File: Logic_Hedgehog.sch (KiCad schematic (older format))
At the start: 65 parts, among them J40 RaspberryPI3, J41 UART_EXT_1, J42 I2C_EXT_0, J43 I2C_EXT_0_EXP, J44 I2C_EXT_1, J45 SPI_EXT_0_0, J46 SPI_EXT_0_1, J47 SPI_EXT_1, J48 Digital, J49 Analog, J50 Digital, J51 Analog, J52 SERVO, J53 SERVO, J54 MOTORS, J55 MOTORS, U40 STM32F401VBT6, U41 74LVC2G32, U42 MC74VHC1G126, U43 IMU_ICM-20689, U44 DRV8835, U45 DRV8835, U46 Buzzer, Y40 Crystal

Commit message: fixed some footprints, should now be correct and complete
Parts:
- C40, C45, C46, C47, C48, C50, C51, C52, C54, C56, C57, C58: footprint Capacitors_SMD:C_0603_HandSoldering -> Capacitors_SMD:C_0603
- C41, C42, C43, C44: footprint Capacitors_SMD:C_0402 -> Capacitors_SMD:C_0603
- C49, C53, C55: footprint Capacitors_SMD:C_0805_HandSoldering -> Capacitors_SMD:C_0805
- J43: footprint (none) -> Socket_Strips:Socket_Strip_Straight_1x04_Pitch2.54mm
- R40, R41, R42, R45, R46, R47, R48, R49, R50: footprint Resistors_SMD:R_0603_HandSoldering -> Resistors_SMD:R_0603
- R44: footprint Resistors_SMD:R_0402 -> Resistors_SMD:R_0603
- U43: footprint hedgehog_footprints:QFN-24_3x3mm -> Housings_DFN_QFN:QFN-24_4x4mm_Pitch0.5mm
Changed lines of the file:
@@
 LIBS:switches
 LIBS:Hedgehog-cache
-EELAYER 25 0
+EELAYER 26 0
 EELAYER END
 $Descr A3 16535 11693
@@
 F 0 "R48" V 11575 1575 50  0000 C CNN
 F 1 "330R" V 11575 1800 50  0000 C CNN
-F 2 "Resistors_SMD:R_0603_HandSoldering" V 11580 1725 50  0001 C CNN
+F 2 "Resistors_SMD:R_0603" V 11580 1725 50  0001 C CNN
 F 3 "" H 11650 1725 50  0001 C CNN
 	1    11650 1725
@@
 F 0 "R47" V 11575 1375 50  0000 C CNN
 F 1 "330R" V 11575 1600 50  0000 C CNN
-F 2 "Resistors_SMD:R_0603_HandSoldering" V 11580 1525 50  0001 C CNN
+F 2 "Resistors_SMD:R_0603" V 11580 1525 50  0001 C CNN
 F 3 "" H 11650 1525 50  0001 C CNN
 	1    11650 1525
@@
 F 0 "C56" V 14700 2575 50  0000 C CNN
 F 1 "1µ" V 14800 2575 50  0000 C CNN
-F 2 "Capacitors_SMD:C_0603_HandSoldering" H 14788 2300 50  0001 C CNN
+F 2 "Capacitors_SMD:C_0603" H 14788 2300 50  0001 C CNN
 F 3 "" H 14750 2450 50  0001 C CNN
 	1    14750 2450
@@
 F 0 "C57" V 14700 4325 50  0000 C CNN
 F 1 "1µ" V 14800 4325 50  0000 C CNN
-F 2 "Capacitors_SMD:C_0603_HandSoldering" H 14788 4050 50  0001 C CNN
+F 2 "Capacitors_SMD:C_0603" H 14788 4050 50  0001 C CNN
 F 3 "" H 14750 4200 50  0001 C CNN
 	1    14750 4200
@@
 F 0 "C58" V 14700 5650 50  0000 C CNN
 F 1 "1µ" V 14800 5650 50  0000 C CNN
-F 2 "Capacitors_SMD:C_0603_HandSoldering" H 14788 5375 50  0001 C CNN
+F 2 "Capacitors_SMD:C_0603" H 14788 5375 50  0001 C CNN
 F 3 "" H 14750 5525 50  0001 C CNN
 	1    14750 5525
@@
 F 0 "R41" H 7400 9925 50  0000 L CNN
 F 1 "R" H 7400 9850 50  0000 L CNN
-F 2 "Resistors_SMD:R_0603_HandSoldering" V 7280 9900 50  0001 C CNN
+F 2 "Resistors_SMD:R_0603" V 7280 9900 50  0001 C CNN
 F 3 "" H 7350 9900 50  0001 C CNN
 	1    7350 9900
@@
 F 0 "R40" H 3800 6575 50  0000 L CNN
 F 1 "R" H 3800 6475 50  0000 L CNN
-F 2 "Resistors_SMD:R_0603_HandSoldering" V 3930 6525 50  0001 C CNN
+F 2 "Resistors_SMD:R_0603" V 3930 6525 50  0001 C CNN
 F 3 "" H 4000 6525 50  0001 C CNN
 	1    4000 6525
@@
 F 0 "R42" H 4325 6425 50  0000 L CNN
 F 1 "22R" H 4325 6350 50  0000 L CNN
-F 2 "Resistors_SMD:R_0603_HandSoldering" V 4455 6400 50  0001 C CNN
+F 2 "Resistors_SMD:R_0603" V 4455 6400 50  0001 C CNN
 F 3 "" H 4525 6400 50  0001 C CNN
 	1    4525 6400
@@
 F 0 "R44" H 4650 6625 50  0000 L CNN
 F 1 "0R" H 4650 6550 50  0000 L CNN
-F 2 "Resistors_SMD:R_0402" V 4555 6400 50  0001 C CNN
+F 2 "Resistors_SMD:R_0603" V 4555 6400 50  0001 C CNN
 F 3 "" H 4625 6400 50  0001 C CNN
 	1    4625 6400
@@
 F 0 "C45" H 4025 7075 50  0000 L CNN
 F 1 "22p" H 4025 7000 50  0000 L CNN
-F 2 "Capacitors_SMD:C_0603_HandSoldering" H 4313 6900 50  0001 C CNN
+F 2 "Capacitors_SMD:C_0603" H 4313 6900 50  0001 C CNN
 F 3 "" H 4275 7050 50  0001 C CNN
 	1    4275 7050
@@
 F 0 "C46" H 4725 7075 50  0000 L CNN
 F 1 "22p" H 4725 7000 50  0000 L CNN
-F 2 "Capacitors_SMD:C_0603_HandSoldering" H 4663 6900 50  0001 C CNN
+F 2 "Capacitors_SMD:C_0603" H 4663 6900 50  0001 C CNN
 F 3 "" H 4625 7050 50  0001 C CNN
 	1    4625 7050
@@
 F 0 "C47" V 5550 1925 50  0000 C CNN
 F 1 "2µ2" V 5550 2125 50  0000 C CNN
-F 2 "Capacitors_SMD:C_0603_HandSoldering" H 5738 1875 50  0001 C CNN
+F 2 "Capacitors_SMD:C_0603" H 5738 1875 50  0001 C CNN
 F 3 "" H 5700 2025 50  0001 C CNN
 	1    5700 2025
@@
 F 0 "C48" V 5650 2100 50  0000 C CNN
 F 1 "2µ2" V 5825 2225 50  0000 C CNN
-F 2 "Capacitors_SMD:C_0603_HandSoldering" H 5738 2075 50  0001 C CNN
+F 2 "Capacitors_SMD:C_0603" H 5738 2075 50  0001 C CNN
 F 3 "" H 5700 2225 50  0001 C CNN
 	1    5700 2225
@@
 F 0 "C44" V 3925 2500 50  0000 L CNN
 F 1 "100n" V 3850 2500 50  0000 L CNN
-F 2 "Capacitors_SMD:C_0402" H 3913 2150 50  0001 C CNN
+F 2 "Capacitors_SMD:C_0603" H 3913 2150 50  0001 C CNN
 F 3 "" H 3875 2300 50  0001 C CNN
 	1    3875 2300
@@
 F 0 "C43" V 3900 2275 50  0000 L CNN
 F 1 "100n" V 3825 2275 50  0000 L CNN
-F 2 "Capacitors_SMD:C_0402" H 3913 1925 50  0001 C CNN
+F 2 "Capacitors_SMD:C_0603" H 3913 1925 50  0001 C CNN
 F 3 "" H 3875 2075 50  0001 C CNN
 	1    3875 2075
@@
 F 0 "C42" V 3900 2050 50  0000 L CNN
 F 1 "100n" V 3825 2050 50  0000 L CNN
-F 2 "Capacitors_SMD:C_0402" H 3913 1700 50  0001 C CNN
+F 2 "Capacitors_SMD:C_0603" H 3913 1700 50  0001 C CNN
 F 3 "" H 3875 1850 50  0001 C CNN
 	1    3875 1850
@@
 F 0 "C41" V 3900 1825 50  0000 L CNN
 F 1 "100n" V 3825 1800 50  0000 L CNN
-F 2 "Capacitors_SMD:C_0402" H 3913 1475 50  0001 C CNN
+F 2 "Capacitors_SMD:C_0603" H 3913 1475 50  0001 C CNN
 F 3 "" H 3875 1625 50  0001 C CNN
 	1    3875 1625
@@
 F 0 "C40" H 1975 1700 50  0000 L CNN
 F 1 "1µ" H 2000 1625 50  0000 L CNN
-F 2 "Capacitors_SMD:C_0603_HandSoldering" H 1913 1500 50  0001 C CNN
+F 2 "Capacitors_SMD:C_0603" H 1913 1500 50  0001 C CNN
 F 3 "" H 1875 1650 50  0001 C CNN
 	1    1875 1650
@@
 F 0 "R50" V 11575 2000 50  0000 C CNN
 F 1 "330R" V 11575 2225 50  0000 C CNN
-F 2 "Resistors_SMD:R_0603_HandSoldering" V 11580 2150 50  0001 C CNN
+F 2 "Resistors_SMD:R_0603" V 11580 2150 50  0001 C CNN
 F 3 "" H 11650 2150 50  0001 C CNN
 	1    11650 2150
@@
 F 0 "R49" V 11575 1800 50  0000 C CNN
 F 1 "330R" V 11575 2025 50  0000 C CNN
-F 2 "Resistors_SMD:R_0603_HandSoldering" V 11580 1950 50  0001 C CNN
+F 2 "Resistors_SMD:R_0603" V 11580 1950 50  0001 C CNN
 F 3 "" H 11650 1950 50  0001 C CNN
 	1    11650 1950
@@
 F 0 "U43" H 9575 10600 60  0000 L CNN
 F 1 "IMU_ICM-20689" H 9100 9675 60  0000 L CNN
-F 2 "hedgehog_footprints:QFN-24_3x3mm" H 10250 9700 60  0001 C CNN
+F 2 "Housings_DFN_QFN:QFN-24_4x4mm_Pitch0.5mm" H 10250 9700 60  0001 C CNN
 F 3 "" H 10250 9700 60  0001 C CNN
 	1    10100 10200
@@
 F 0 "C51" H 8900 10400 50  0000 L CNN
 F 1 "0µ47" H 8850 10575 50  0000 L CNN
-F 2 "Capacitors_SMD:C_0603_HandSoldering" H 9113 10325 50  0001 C CNN
+F 2 "Capacitors_SMD:C_0603" H 9113 10325 50  0001 C CNN
 F 3 "" H 9075 10475 50  0001 C CNN
 	1    9075 10475
@@
 F 0 "C50" H 8975 10200 50  0000 L CNN
 F 1 "2µ2" H 8975 10375 50  0000 L CNN
-F 2 "Capacitors_SMD:C_0603_HandSoldering" H 8988 10125 50  0001 C CNN
+F 2 "Capacitors_SMD:C_0603" H 8988 10125 50  0001 C CNN
 F 3 "" H 8950 10275 50  0001 C CNN
 	1    8950 10275
@@
 F 0 "C49" H 8800 10200 50  0000 L CNN
 F 1 "100n" H 8750 10375 50  0000 L CNN
-F 2 "Capacitors_SMD:C_0805_HandSoldering" H 8763 10125 50  0001 C CNN
+F 2 "Capacitors_SMD:C_0805" H 8763 10125 50  0001 C CNN
 F 3 "" H 8725 10275 50  0001 C CNN
 	1    8725 10275
@@
 F 0 "R46" H 10175 5125 50  0000 C CNN
 F 1 "1k8" H 10150 5200 50  0000 C CNN
-F 2 "Resistors_SMD:R_0603_HandSoldering" V 10205 5175 50  0001 C CNN
+F 2 "Resistors_SMD:R_0603" V 10205 5175 50  0001 C CNN
 F 3 "" H 10275 5175 50  0001 C CNN
 	1    10275 5175
@@
 F 0 "R45" H 10300 5125 50  0000 C CNN
 F 1 "1k8" H 10300 5200 50  0000 C CNN
-F 2 "Resistors_SMD:R_0603_HandSoldering" V 10105 5175 50  0001 C CNN
+F 2 "Resistors_SMD:R_0603" V 10105 5175 50  0001 C CNN
 F 3 "" H 10175 5175 50  0001 C CNN
 	1    10175 5175
@@
 F 0 "C53" H 13100 7325 50  0000 L CNN
 F 1 "100n" H 13100 7175 50  0000 L CNN
-F 2 "Capacitors_SMD:C_0805_HandSoldering" H 13113 7100 50  0001 C CNN
+F 2 "Capacitors_SMD:C_0805" H 13113 7100 50  0001 C CNN
 F 3 "" H 13075 7250 50  0001 C CNN
 	1    13075 7250
@@
 F 0 "C55" H 13100 8450 50  0000 L CNN
 F 1 "100n" H 13100 8300 50  0000 L CNN
-F 2 "Capacitors_SMD:C_0805_HandSoldering" H 13113 8225 50  0001 C CNN
+F 2 "Capacitors_SMD:C_0805" H 13113 8225 50  0001 C CNN
 F 3 "" H 13075 8375 50  0001 C CNN
 	1    13075 8375
@@
 F 0 "C52" H 12725 7325 50  0000 L CNN
 F 1 "10µ" H 12725 7175 50  0000 L CNN
-F 2 "Capacitors_SMD:C_0603_HandSoldering" H 12738 7100 50  0001 C CNN
+F 2 "Capacitors_SMD:C_0603" H 12738 7100 50  0001 C CNN
 F 3 "" H 12700 7250 50  0001 C CNN
 	1    12700 7250
@@
 F 0 "C54" H 12725 8450 50  0000 L CNN
 F 1 "10µ" H 12725 8300 50  0000 L CNN
-F 2 "Capacitors_SMD:C_0603_HandSoldering" H 12738 8225 50  0001 C CNN
+F 2 "Capacitors_SMD:C_0603" H 12738 8225 50  0001 C CNN
 F 3 "" H 12700 8375 50  0001 C CNN
 	1    12700 8375
@@
 F 0 "J43" H 11377 4816 50  0000 L CNN
 F 1 "I2C_EXT_0_EXP" H 11377 4725 50  0000 L CNN
-F 2 "" H 11300 4775 50  0001 C CNN
+F 2 "Socket_Strips:Socket_Strip_Straight_1x04_Pitch2.54mm" H 11300 4775 50  0001 C CNN
 F 3 "" H 11300 4775 50  0001 C CNN
 	1    11300 4775

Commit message: started layout
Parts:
- added C61, C62: 100n, Capacitors_SMD:C_0603, symbol C
- J54, J55: footprint Socket_Strips:Socket_Strip_Angled_1x04_Pitch2.54mm -> Pin_Headers:Pin_Header_Straight_1x04_Pitch2.54mm
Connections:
- net +3V3: now also C61.1, C62.1
- net GND: now also C61.2, C62.2
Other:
- note added: "Ref: 4x, 5x, 6x"
- note removed: "Ref: 4x, 5x"
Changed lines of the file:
@@
 Text Notes 7775 4900 1    60   ~ 0
 PullUp/DigIn
-Text Notes 15025 9900 0    118  ~ 0
-Ref: 4x, 5x
+Text Notes 14675 9925 0    118  ~ 0
+Ref: 4x, 5x, 6x
 $Comp
 L C C56
@@
 F 0 "J55" H 15350 7650 50  0000 R CNN
 F 1 "MOTORS" V 15375 7550 50  0000 R CNN
-F 2 "Socket_Strips:Socket_Strip_Angled_1x04_Pitch2.54mm" H 15275 7400 50  0001 C CNN
+F 2 "Pin_Headers:Pin_Header_Straight_1x04_Pitch2.54mm" H 15275 7400 50  0001 C CNN
 F 3 "" H 15275 7400 50  0001 C CNN
 	1    15275 7400
@@
 F 0 "J54" H 15075 7650 50  0000 R CNN
 F 1 "MOTORS" V 15100 7550 50  0000 R CNN
-F 2 "Socket_Strips:Socket_Strip_Angled_1x04_Pitch2.54mm" H 15000 7400 50  0001 C CNN
+F 2 "Pin_Headers:Pin_Header_Straight_1x04_Pitch2.54mm" H 15000 7400 50  0001 C CNN
 F 3 "" H 15000 7400 50  0001 C CNN
 	1    15000 7400
@@
 NoConn ~ 6875 5025
 NoConn ~ 6875 3325
+$Comp
+L C C62
+U 1 1 592842EA
+P 4250 2000
+F 0 "C62" V 4300 1800 50  0000 L CNN
+F 1 "100n" V 4175 1750 50  0000 L CNN
+F 2 "Capacitors_SMD:C_0603" H 4288 1850 50  0001 C CNN
+F 3 "" H 4250 2000 50  0001 C CNN
+	1    4250 2000
+	0    -1   -1   0
+$EndComp
+$Comp
+L C C61
+U 1 1 592843C6
+P 4250 1775
+F 0 "C61" V 4300 1575 50  0000 L CNN
+F 1 "100n" V 4175 1525 50  0000 L CNN
+F 2 "Capacitors_SMD:C_0603" H 4288 1625 50  0001 C CNN
+F 3 "" H 4250 1775 50  0001 C CNN
+	1    4250 1775
+	0    -1   -1   0
+$EndComp
+Wire Wire Line
+	4100 1775 4050 1775
+Connection ~ 4050 1775
+Wire Wire Line
+	4100 2000 4050 2000
+Connection ~ 4050 2000
+Wire Wire Line
+	4400 1775 4550 1775
+Wire Wire Line
+	4550 1775 4550 2050
+Wire Wire Line
+	4550 2000 4400 2000
+$Comp
+L GND #PWR066
+U 1 1 5928516D
+P 4550 2050
+F 0 "#PWR066" H 4550 1800 50  0001 C CNN
+F 1 "GND" H 4550 1900 50  0000 C CNN
+F 2 "" H 4550 2050 50  0001 C CNN
+F 3 "" H 4550 2050 50  0001 C CNN
+	1    4550 2050
+	1    0    0    -1
+$EndComp
+Connection ~ 4550 2000
 $EndSCHEMATC

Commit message: more layouting done, schematic changed slightly
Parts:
- added C63: 100n, Capacitors_SMD:C_0603, symbol C
- C49, C53, C55: footprint Capacitors_SMD:C_0805 -> Capacitors_SMD:C_0603
- J54, J55: footprint Pin_Headers:Pin_Header_Straight_1x04_Pitch2.54mm -> Socket_Strips:Socket_Strip_Straight_1x04_Pitch2.54mm
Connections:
- net +5V: now also J53.2 (P2), J53.4 (P4), J53.6 (P6), J53.8 (P8); no longer J53.1 (P1), J53.3 (P3), J53.5 (P5), J53.7 (P7)
- net ANALOG_0: now also U40.88 (PD7); no longer U40.81 (PD0)
- net ANALOG_1: now also U40.87 (PD6); no longer U40.82 (PD1)
- net ANALOG_2: now also U40.86 (PD5); no longer U40.83 (PD2)
- net ANALOG_3: now also U40.85 (PD4); no longer U40.84 (PD3)
- net ANALOG_4: now also U40.84 (PD3); no longer U40.85 (PD4)
- net ANALOG_5: now also U40.83 (PD2); no longer U40.86 (PD5)
- net ANALOG_6: now also U40.82 (PD1); no longer U40.87 (PD6)
- net ANALOG_7: now also U40.81 (PD0)
- net GND: now also J53.1 (P1), J53.3 (P3), J53.5 (P5), J53.7 (P7), C63.1; no longer J53.2 (P2), J53.4 (P4), J53.6 (P6), J53.8 (P8)
- net LED_3: now also J40.40 (GPIO21); no longer J40.38 (GPIO20)
- net LED_4: now also J40.38 (GPIO20); no longer J40.40 (GPIO21)
- net VDDA: now also C63.2
- no-connect marks 19 -> 18
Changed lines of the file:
@@
 F 3 "" H 14750 4000 50  0001 C CNN
 	1    14750 5200
-	1    0    0    -1
+	-1   0    0    -1
 $EndComp
 $Comp
@@
 L VDDA #PWR034
 U 1 1 5915AE39
-P 5125 2025
-F 0 "#PWR034" H 5125 1875 50  0001 C CNN
-F 1 "VDDA" H 5142 2198 50  0000 C CNN
-F 2 "" H 5125 2025 50  0001 C CNN
-F 3 "" H 5125 2025 50  0001 C CNN
-	1    5125 2025
+P 5125 1825
+F 0 "#PWR034" H 5125 1675 50  0001 C CNN
+F 1 "VDDA" H 5142 1998 50  0000 C CNN
+F 2 "" H 5125 1825 50  0001 C CNN
+F 3 "" H 5125 1825 50  0001 C CNN
+	1    5125 1825
 	1    0    0    -1
 $EndComp
@@
 LED_4
 Text Label 4225 10300 2    60   ~ 0
+LED_4
+Text Label 4225 10400 2    60   ~ 0
 LED_3
-Text Label 4225 10400 2    60   ~ 0
-LED_4
 Text Label 1275 10000 0    60   ~ 0
 STM_BOOT0
@@
 F 0 "C49" H 8800 10200 50  0000 L CNN
 F 1 "100n" H 8750 10375 50  0000 L CNN
-F 2 "Capacitors_SMD:C_0805" H 8763 10125 50  0001 C CNN
+F 2 "Capacitors_SMD:C_0603" H 8763 10125 50  0001 C CNN
 F 3 "" H 8725 10275 50  0001 C CNN
 	1    8725 10275
@@
 Text Label 2875 4325 0    60   ~ 0
 ANALOG_7
-Text Label 7625 4325 2    60   ~ 0
+Text Label 7625 4425 2    60   ~ 0
+ANALOG_6
+Text Label 7625 4525 2    60   ~ 0
+ANALOG_5
+Text Label 7625 4625 2    60   ~ 0
+ANALOG_4
+Text Label 7625 4725 2    60   ~ 0
+ANALOG_3
+Text Label 7625 4825 2    60   ~ 0
+ANALOG_2
+Text Label 7625 4925 2    60   ~ 0
+ANALOG_1
+Text Label 7625 5025 2    60   ~ 0
 ANALOG_0
-Text Label 7625 4425 2    60   ~ 0
-ANALOG_1
-Text Label 7625 4525 2    60   ~ 0
-ANALOG_2
-Text Label 7625 4625 2    60   ~ 0
-ANALOG_3
-Text Label 7625 4725 2    60   ~ 0
-ANALOG_4
-Text Label 7625 4825 2    60   ~ 0
-ANALOG_5
-Text Label 7625 4925 2    60   ~ 0
-ANALOG_6
 Text Label 13550 3325 0    60   ~ 0
 ANALOG_0
@@
 Connection ~ 1875 1425
 Wire Wire Line
-	5125 2025 5125 2325
+	5125 1825 5125 2325
 Wire Wire Line
 	3725 3625 2875 3625
@@
 	14000 3925 13550 3925
 Wire Notes Line
-	7675 4200 7675 5000
-Wire Notes Line
-	7675 5000 7125 5000
-Wire Notes Line
-	7125 5000 7125 4200
+	7675 4200 7675 5050
+Wire Notes Line
+	7125 4200 7125 5050
 Wire Notes Line
 	7125 4200 7675 4200
@@
 F 0 "C53" H 13100 7325 50  0000 L CNN
 F 1 "100n" H 13100 7175 50  0000 L CNN
-F 2 "Capacitors_SMD:C_0805" H 13113 7100 50  0001 C CNN
+F 2 "Capacitors_SMD:C_0603" H 13113 7100 50  0001 C CNN
 F 3 "" H 13075 7250 50  0001 C CNN
 	1    13075 7250
@@
 F 0 "C55" H 13100 8450 50  0000 L CNN
 F 1 "100n" H 13100 8300 50  0000 L CNN
-F 2 "Capacitors_SMD:C_0805" H 13113 8225 50  0001 C CNN
+F 2 "Capacitors_SMD:C_0603" H 13113 8225 50  0001 C CNN
 F 3 "" H 13075 8375 50  0001 C CNN
 	1    13075 8375
@@
 F 0 "J55" H 15350 7650 50  0000 R CNN
 F 1 "MOTORS" V 15375 7550 50  0000 R CNN
-F 2 "Pin_Headers:Pin_Header_Straight_1x04_Pitch2.54mm" H 15275 7400 50  0001 C CNN
+F 2 "Socket_Strips:Socket_Strip_Straight_1x04_Pitch2.54mm" H 15275 7400 50  0001 C CNN
 F 3 "" H 15275 7400 50  0001 C CNN
 	1    15275 7400
@@
 F 0 "J54" H 15075 7650 50  0000 R CNN
 F 1 "MOTORS" V 15100 7550 50  0000 R CNN
-F 2 "Pin_Headers:Pin_Header_Straight_1x04_Pitch2.54mm" H 15000 7400 50  0001 C CNN
+F 2 "Socket_Strips:Socket_Strip_Straight_1x04_Pitch2.54mm" H 15000 7400 50  0001 C CNN
 F 3 "" H 15000 7400 50  0001 C CNN
 	1    15000 7400
@@
 NoConn ~ 6225 6125
 NoConn ~ 6325 6125
-NoConn ~ 6875 5025
 NoConn ~ 6875 3325
 $Comp
@@
 $EndComp
 Connection ~ 4550 2000
+$Comp
+L C C63
+U 1 1 592E5E7B
+P 4775 1950
+F 0 "C63" V 4825 1750 50  0000 L CNN
+F 1 "100n" V 4700 1700 50  0000 L CNN
+F 2 "Capacitors_SMD:C_0603" H 4813 1800 50  0001 C CNN
+F 3 "" H 4775 1950 50  0001 C CNN
+	1    4775 1950
+	0    -1   -1   0
+$EndComp
+Wire Wire Line
+	4925 1950 5125 1950
+Connection ~ 5125 1950
+Wire Wire Line
+	4625 1950 4550 1950
+Connection ~ 4550 1950
+Wire Wire Line
+	6875 5025 7625 5025
+Text Label 7625 4325 2    60   ~ 0
+ANALOG_7
+Wire Notes Line
+	7125 5050 7675 5050
 $EndSCHEMATC

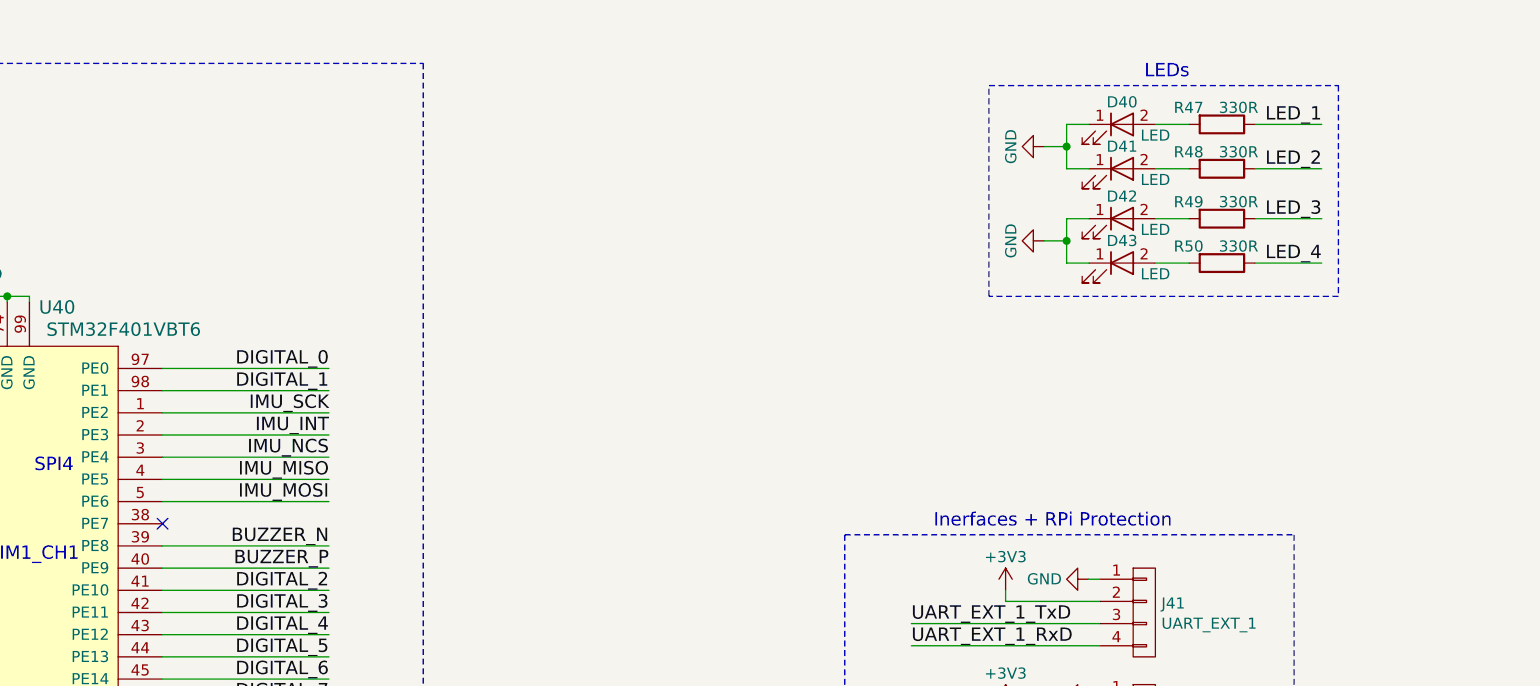
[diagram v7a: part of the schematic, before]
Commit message: more layouting done, just regulators missing
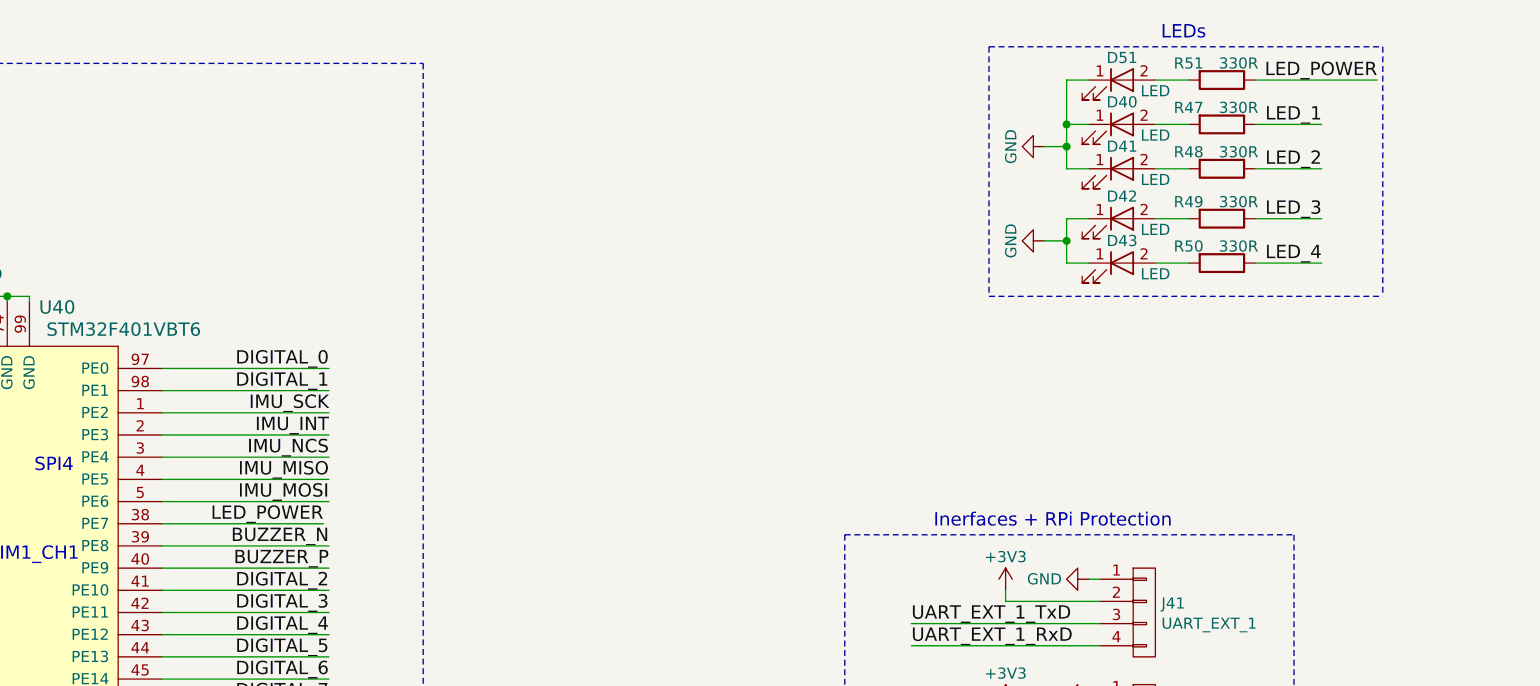
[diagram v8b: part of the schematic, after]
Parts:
- added D51: LED, LEDs:LED_0805, symbol LED
- added R51: 330R, Resistors_SMD:R_0603, symbol R
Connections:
- net GND: now also D51.1 (K)
- net LED_POWER: now reaches U40.38 (PE7)
- net LED_POWER: now also R51.1
- new net: D51.2 (A), R51.2
- no-connect marks 18 -> 17
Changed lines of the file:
@@
 Text Notes 9875 9550 0    60   ~ 0
 IMU
-Text Notes 11300 1325 0    60   ~ 0
+Text Notes 11375 1150 0    60   ~ 0
 LEDs
 Text Notes 13825 9050 0    60   ~ 0
@@
 	10850 1625 10950 1625
 Wire Wire Line
-	10950 1525 10950 1725
+	10950 1325 10950 1725
 Wire Wire Line
 	10950 1525 11050 1525
@@
 	8475 9550 11475 9550
 Wire Notes Line
-	12175 1350 12175 2300
-Wire Notes Line
-	12175 2300 10600 2300
-Wire Notes Line
-	10600 2300 10600 1350
-Wire Notes Line
-	10600 1350 12175 1350
+	10600 2300 12375 2300
+Wire Notes Line
+	10600 1175 10600 2300
 Wire Notes Line
 	14625 9075 14625 9675
@@
 NoConn ~ 6225 6125
 NoConn ~ 6325 6125
-NoConn ~ 6875 3325
 $Comp
 L C C62
@@
 Wire Notes Line
 	7125 5050 7675 5050
+Text Label 7600 3325 2    60   ~ 0
+LED_POWER
+Wire Wire Line
+	7600 3325 6875 3325
+Text Label 12350 1325 2    60   ~ 0
+LED_POWER
+$Comp
+L LED D51
+U 1 1 59308F2C
+P 11200 1325
+F 0 "D51" H 11200 1425 50  0000 C CNN
+F 1 "LED" H 11350 1275 50  0000 C CNN
+F 2 "LEDs:LED_0805" H 11200 1325 50  0001 C CNN
+F 3 "" H 11200 1325 50  0001 C CNN
+	1    11200 1325
+	1    0    0    -1
+$EndComp
+$Comp
+L R R51
+U 1 1 59308FD2
+P 11650 1325
+F 0 "R51" V 11575 1175 50  0000 C CNN
+F 1 "330R" V 11575 1400 50  0000 C CNN
+F 2 "Resistors_SMD:R_0603" V 11580 1325 50  0001 C CNN
+F 3 "" H 11650 1325 50  0001 C CNN
+	1    11650 1325
+	0    1    1    0
+$EndComp
+Wire Wire Line
+	11050 1325 10950 1325
+Connection ~ 10950 1525
+Wire Wire Line
+	11350 1325 11500 1325
+Wire Wire Line
+	11800 1325 12350 1325
+Wire Notes Line
+	10600 1175 12375 1175
+Wire Notes Line
+	12375 1175 12375 2300
 $EndSCHEMATC
